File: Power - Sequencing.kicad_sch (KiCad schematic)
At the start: 0 parts

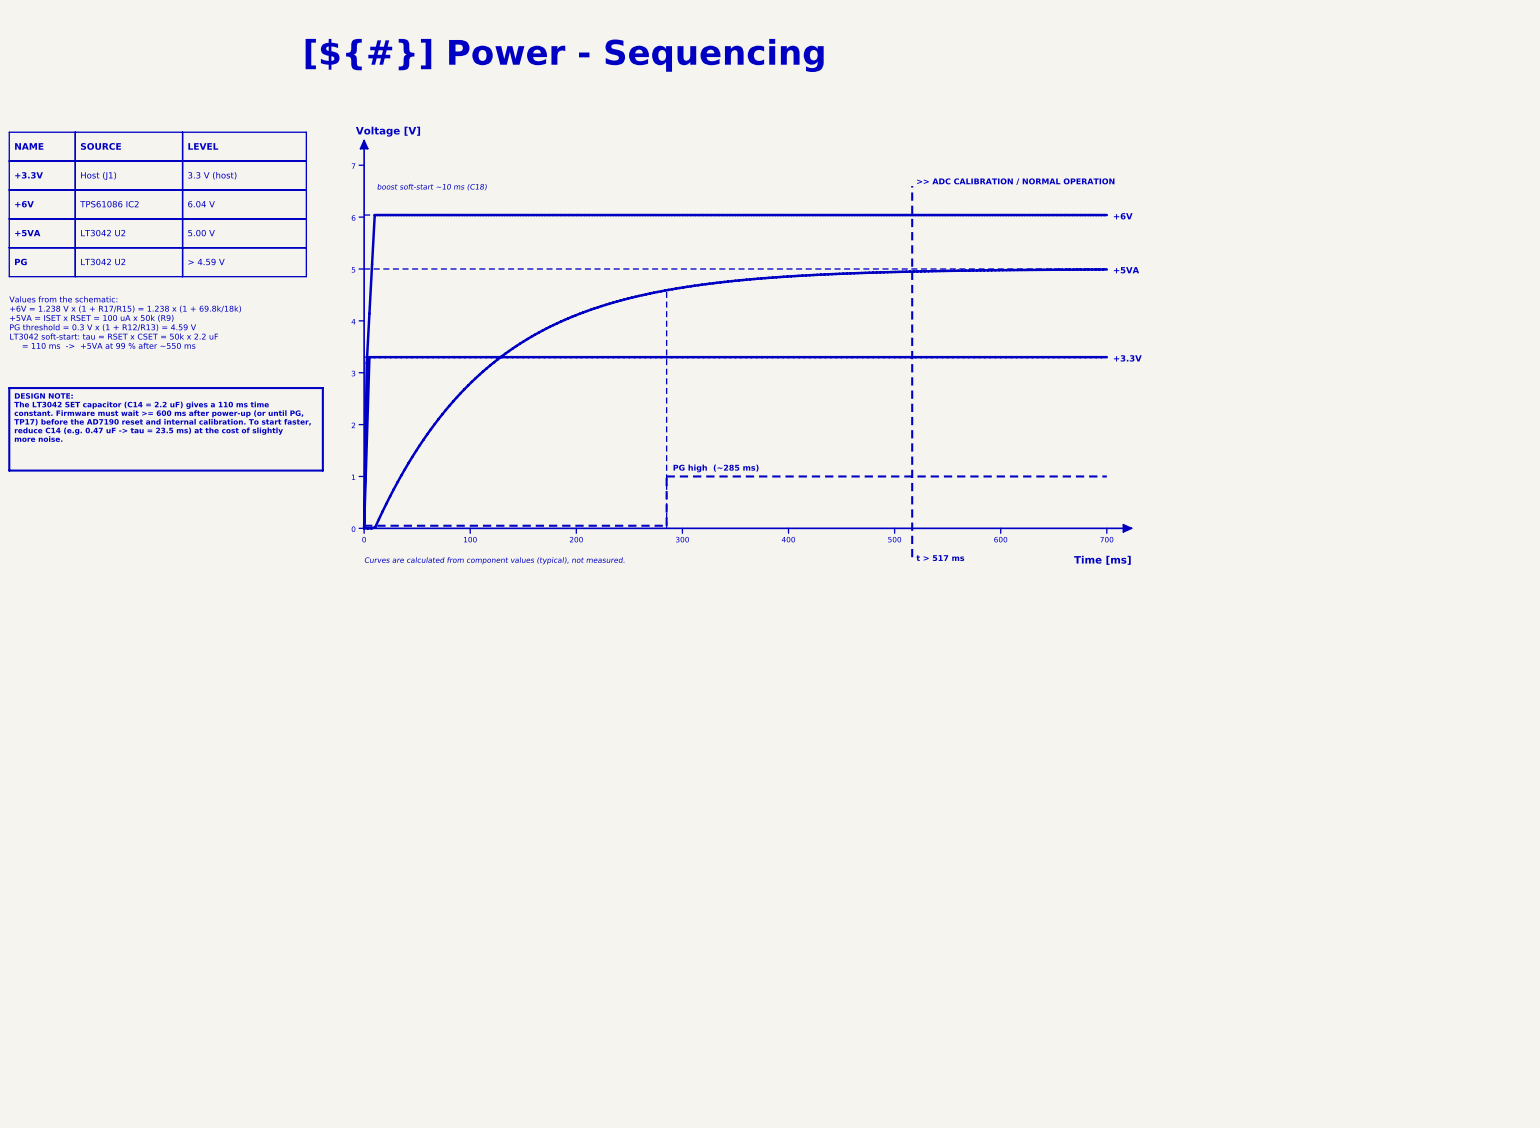
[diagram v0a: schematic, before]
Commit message: Restyle the schematic like OPEN_PHASE, merge the power sheets, rework the bottom silkscreen
- Schematic: all sheets on A3 in the OPEN_PHASE look (red header bands,
  DESCRIPTION / DESIGN NOTE / LAYOUT NOTE / CALCULS & BUDGET panels in
  French, TEST POINTS panel, References in the title block)
- Title block: INGENIERIE FRANCE logo in KDT_Template_GIT.kicad_wks,
  per-sheet logo images removed
- Power - Sequencing rebuilt with curves from LTspice simulations 01-04
- TPS61086 and LT3042 sheets merged into Power Supply - Analog Rails
  (page 5, keeps the TPS sheet UUID); pages renumbered to 9, local nets
  renamed to /Project Architecture/Power_Supply/*, PCB links updated
- PCB: per-rail net colours (+3.3V, +6V, +5VA, GND) as on OPEN_PHASE
- PCB B.SilkS: test point pills with Arial Black knockout names, J1
  pinout cells, E+/E-/S+/S- tags on the M12 pads, CELL 1 / CELL 2 titles
  and a LOAD CELL wiring panel

Netlist connectivity, ERC (2 warnings) and copper DRC unchanged;
schematic parity clean.

Co-Authored-By: Claude Opus 5.5 <noreply@anthropic.com>
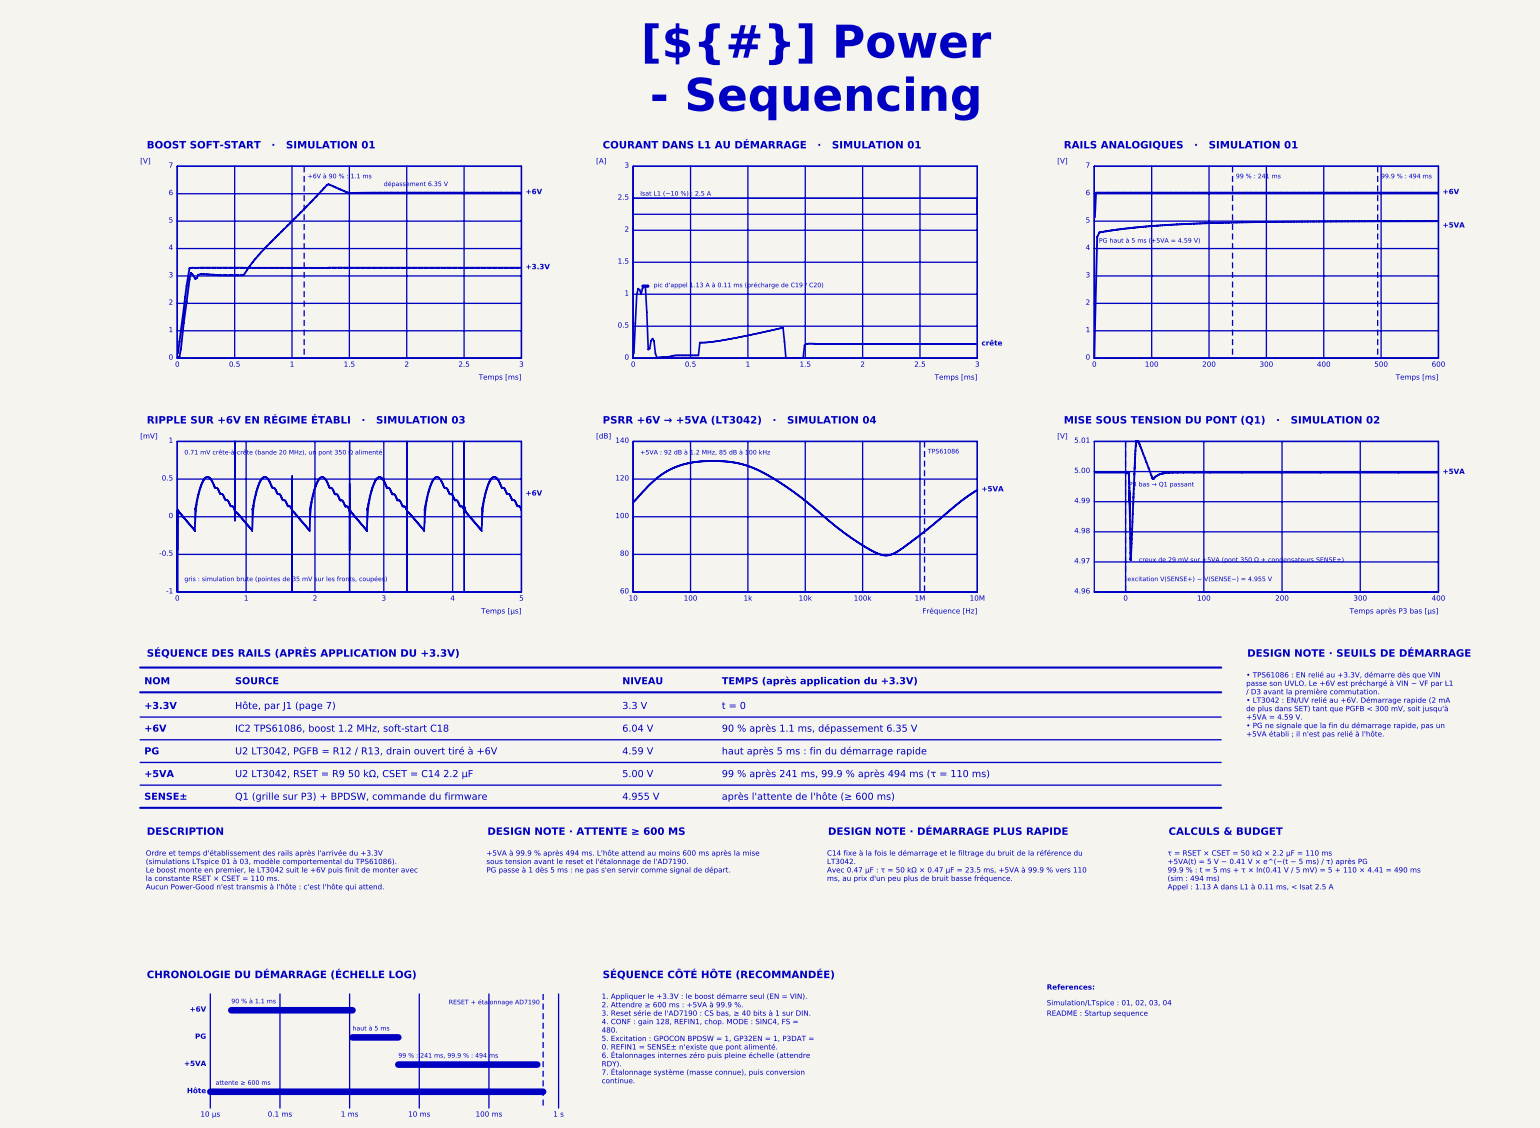
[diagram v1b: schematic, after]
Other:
- note added: "+5VA : 92 dB à 1.2 MHz, 85 dB à 100 kHz"
- note added: "+6V à 90 % : 1.1 ms"
- note added: "-0.5"
- note added: "-1"
- note added: "0.1 ms"
- note added: "0.5"
- note added: "0.71 mV crête-à-crête (bande 20 MHz), un pont 350 Ω alimenté"
- note added: "1 ms"
- note added: "1 s"
- note added: "1.5"
- note added: "10"
- note added: "10 ms"
- note added: "10 µs"
- note added: "100 ms"
- note added: "100k"
- note added: "10M"
- note added: "10k"
- note added: "120"
- note added: "140"
- note added: "1M"
- note added: "1k"
- note added: "2.5"
- note added: "3.3 V"
- note added: "4.59 V"
- note added: "4.955 V"
- note added: "4.96"
- note added: "4.97"
- note added: "4.98"
- note added: "4.99"
- note added: "5.00"
- note added: "5.00 V"
- note added: "5.01"
- note added: "6.04 V"
- note added: "60"
- note added: "80"
- note added: "90 % après 1.1 ms, dépassement 6.35 V"
- note added: "90 % à 1.1 ms"
- note added: "99 % : 241 ms"
- note added: "99 % : 241 ms, 99.9 % : 494 ms"
- note added: "99 % après 241 ms, 99.9 % après 494 ms (τ = 110 ms)"
- note added: "99.9 % : 494 ms"
- note added: "Fréquence [Hz]"
- note added: "Hôte"
- note added: "Hôte, par J1 (page 7)"
- note added: "IC2 TPS61086, boost 1.2 MHz, soft-start C18"
- note added: "Isat L1 (−10 %) : 2.5 A"
- note added: "NIVEAU"
- note added: "NOM"
- note added: "P3 bas → Q1 passant"
- note added: "PG"
- note added: "PG haut à 5 ms (+5VA = 4.59 V)"
- note added: "Q1 (grille sur P3) + BPDSW, commande du firmware"
- note added: "README : Startup sequence"
- note added: "RESET + étalonnage AD7190"
- note added: "References:"
- note added: "SENSE±"
- note added: "SOURCE"
- note added: "Simulation/LTspice : 01, 02, 03, 04"
- note added: "TEMPS (après application du +3.3V)"
- note added: "TPS61086"
- note added: "Temps [ms]"
- note added: "Temps [µs]"
- note added: "Temps après P3 bas [µs]"
- note added: "U2 LT3042, PGFB = R12 / R13, drain ouvert tiré à +6V"
- note added: "U2 LT3042, RSET = R9 50 kΩ, CSET = C14 2.2 µF"
- note added: "[A]"
- note added: "[V]"
- note added: "[dB]"
- note added: "[mV]"
- note added: "après l'attente de l'hôte (≥ 600 ms)"
- note added: "attente ≥ 600 ms"
- note added: "creux de 29 mV sur +5VA (pont 350 Ω + condensateurs SENSE±)"
- note added: "crête"
- note added: "dépassement 6.35 V"
- note added: "excitation V(SENSE+) − V(SENSE−) = 4.955 V"
- note added: "gris : simulation brute (pointes de 35 mV sur les fronts, coupées)"
- note added: "haut après 5 ms : fin du démarrage rapide"
- note added: "haut à 5 ms"
- note added: "pic d'appel 1.13 A à 0.11 ms (précharge de C19 / C20)"
- note added: "t = 0"
- note removed: "700"
- note removed: ">> ADC CALIBRATION / NORMAL OPERATION"
- note removed: "Curves are calculated from component values (typical), not measured."
- note removed: "PG high (~285 ms)"
- note removed: "Time [ms]"
- note removed: "Values from the schematic: +6V = 1.238 V x (1 + R17/R15) = 1.238 x (1 + 69.8k/18k) +5VA = ISET x RSET = 100 uA x 50k (R9) PG threshold = 0.3 V x (1 + R12/R13) = 4.59 V LT3042 soft-start: tau = RSET x CSET = 50k x 2.2 uF = 110 ms -> +5VA at 99 % after ~550 ms"
- note removed: "Voltage [V]"
- note removed: "boost soft-start ~10 ms (C18)"
- note removed: "t > 517 ms"
